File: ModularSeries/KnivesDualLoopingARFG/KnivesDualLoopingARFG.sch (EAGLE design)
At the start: 73 parts, among them P1 2XWIREPAD, P2 2XWIREPAD, P3 2XWIREPAD, P4 2XWIREPAD, Q1 2N3904, Q2 2N3904

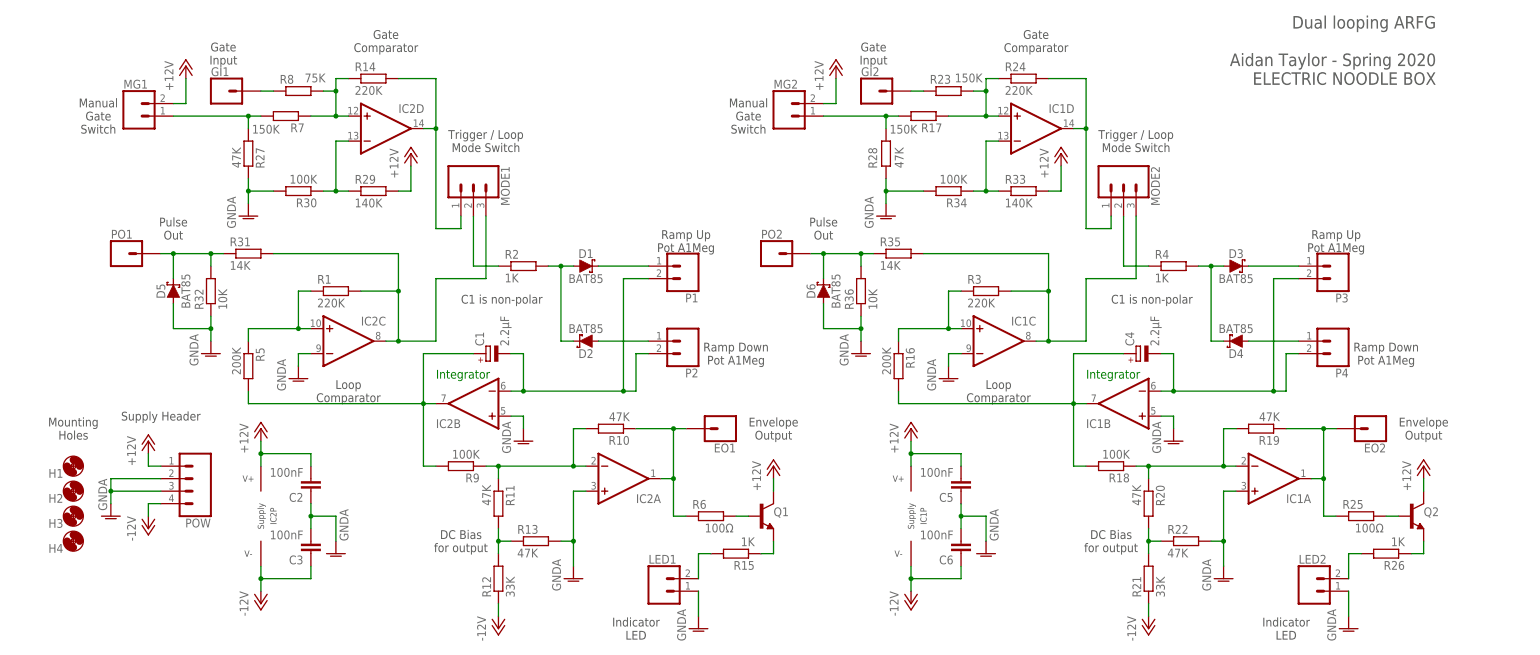
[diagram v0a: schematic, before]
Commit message: Power header updated on most PCBs. Knives layout added
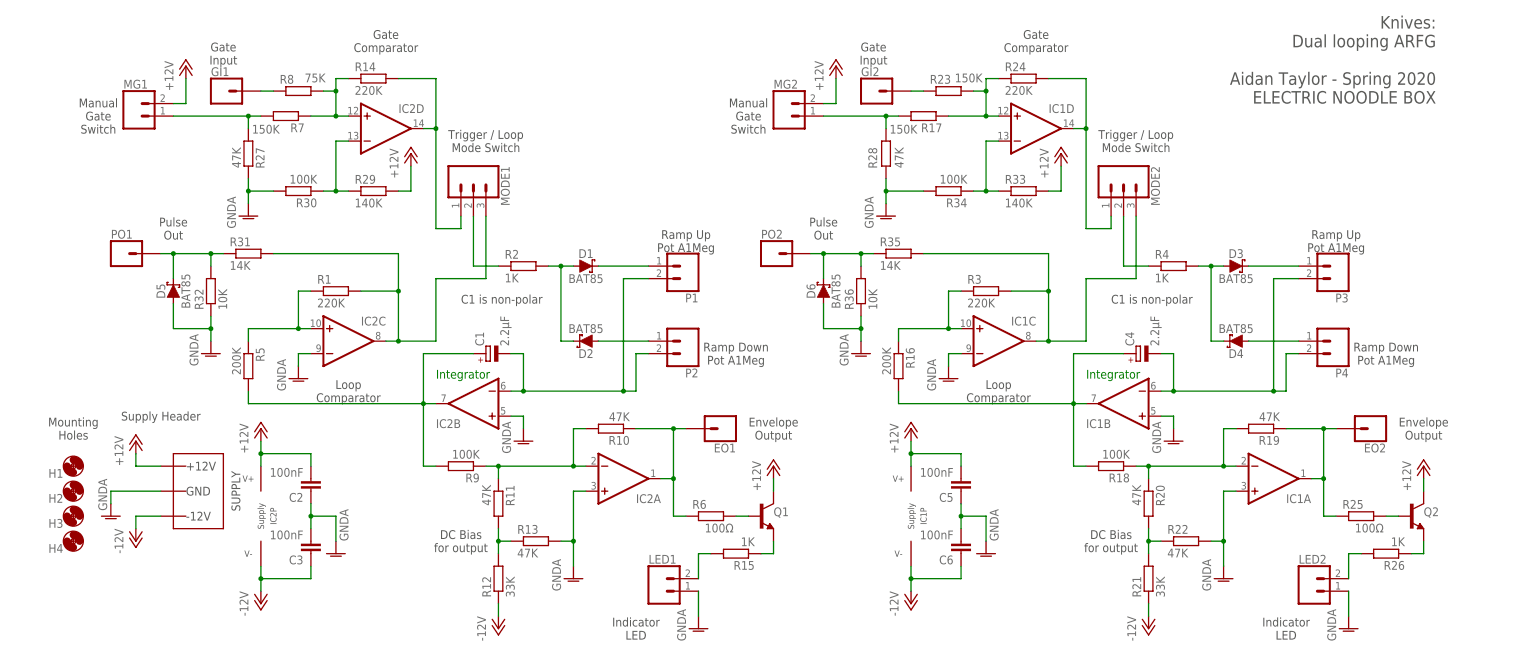
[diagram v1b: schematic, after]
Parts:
- removed POW: 4XMOLEX, ElectricNoodleBox:4XMOLEX
- added WP1: COMBO_SUPPLY_HEADER, ElectricNoodleBox:COMBO_SUPPLY_HEADER
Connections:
- net +12V: now also WP1.V++; no longer POW.1
- net -12V: now also WP1.V--; no longer POW.4
- net GNDA: now also WP1.AGND; no longer POW.2, POW.3
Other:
- note added: "Knives: Dual looping ARFG Aidan Taylor - Spring 2020 ELECTRIC NOODLE BOX"
- note removed: "Dual looping ARFG Aidan Taylor - Spring 2020 ELECTRIC NOODLE BOX"
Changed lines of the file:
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@@
 <part name="LED2" library="ElectricNoodleBox" deviceset="2XWIREPAD" device=""/>
 <part name="IC1" library="ElectricNoodleBox" deviceset="TL0X4" device="DIL" package3d_urn="urn:adsk.eagle:package:16407/2"/>
-<part name="POW" library="ElectricNoodleBox" deviceset="4XMOLEX" device="">
-<attribute name="SPICEPREFIX" value="E"/>
-</part>
 <part name="P+7" library="supply1" library_urn="urn:adsk.eagle:library:371" deviceset="+12V" device="">
 <attribute name="SPICEPREFIX" value="G"/>
@@
 <part name="GND5" library="supply1" library_urn="urn:adsk.eagle:library:371" deviceset="GNDA" device=""/>
 <part name="D6" library="ElectricNoodleBox" deviceset="SCHOTTKY_DO35" device="" package3d_urn="urn:adsk.eagle:package:43339/2" value="BAT85"/>
+<part name="WP1" library="ElectricNoodleBox" deviceset="COMBO_SUPPLY_HEADER" device=""/>
 </parts>
 <sheets>
@@
 <text x="271.78" y="50.8" size="1.778" layer="97" align="center">Envelope
 Output</text>
-<text x="274.32" y="134.62" size="2.54" layer="97" align="top-right">Dual looping ARFG
+<text x="274.32" y="134.62" size="2.54" layer="97" align="top-right">Knives:
+Dual looping ARFG
 Aidan Taylor - Spring 2020
 ELECTRIC NOODLE BOX</text>
@@
 <attribute name="NAME" x="170.18" y="33.02" size="1.27" layer="97" rot="R90" align="center"/>
 </instance>
-<instance part="POW" gate="G$1" x="20.32" y="40.64" smashed="yes" rot="R180">
-<attribute name="NAME" x="25.4" y="32.512" size="1.778" layer="95" font="vector" rot="R180"/>
-</instance>
-<instance part="P+7" gate="1" x="12.7" y="48.26" smashed="yes">
-<attribute name="VALUE" x="10.16" y="43.18" size="1.778" layer="96" rot="R90"/>
-</instance>
-<instance part="P-7" gate="1" x="12.7" y="30.48" smashed="yes">
-<attribute name="VALUE" x="10.16" y="27.94" size="1.778" layer="96" rot="R90"/>
+<instance part="P+7" gate="1" x="10.16" y="48.26" smashed="yes">
+<attribute name="VALUE" x="7.62" y="43.18" size="1.778" layer="96" rot="R90"/>
+</instance>
+<instance part="P-7" gate="1" x="10.16" y="27.94" smashed="yes">
+<attribute name="VALUE" x="7.62" y="25.4" size="1.778" layer="96" rot="R90"/>
 </instance>
 <instance part="GND13" gate="1" x="5.08" y="33.02" smashed="yes">
@@
 <attribute name="VALUE" x="152.4" y="78.74" size="1.778" layer="96" font="vector" rot="R90" align="center"/>
 </instance>
+<instance part="WP1" gate="G$1" x="22.86" y="38.1" smashed="yes"/>
 </instances>
 <busses>
@@
 </segment>
 <segment>
-<pinref part="POW" gate="G$1" pin="2"/>
-<wire x1="15.24" y1="40.64" x2="5.08" y2="40.64" width="0.1524" layer="91"/>
 <pinref part="GND13" gate="1" pin="GNDA"/>
-<wire x1="5.08" y1="40.64" x2="5.08" y2="38.1" width="0.1524" layer="91"/>
-<pinref part="POW" gate="G$1" pin="3"/>
 <wire x1="5.08" y1="38.1" x2="5.08" y2="35.56" width="0.1524" layer="91"/>
 <wire x1="15.24" y1="38.1" x2="5.08" y2="38.1" width="0.1524" layer="91"/>
-<junction x="5.08" y="38.1"/>
+<pinref part="WP1" gate="G$1" pin="AGND"/>
 </segment>
 <segment>
@@
 </segment>
 <segment>
-<pinref part="POW" gate="G$1" pin="4"/>
-<wire x1="15.24" y1="35.56" x2="12.7" y2="35.56" width="0.1524" layer="91"/>
+<wire x1="15.24" y1="33.02" x2="10.16" y2="33.02" width="0.1524" layer="91"/>
 <pinref part="P-7" gate="1" pin="-12V"/>
-<wire x1="12.7" y1="35.56" x2="12.7" y2="33.02" width="0.1524" layer="91"/>
+<wire x1="10.16" y1="33.02" x2="10.16" y2="30.48" width="0.1524" layer="91"/>
+<pinref part="WP1" gate="G$1" pin="V--"/>
 </segment>
 </net>
@@
 </segment>
 <segment>
-<pinref part="POW" gate="G$1" pin="1"/>
-<wire x1="15.24" y1="43.18" x2="12.7" y2="43.18" width="0.1524" layer="91"/>
+<wire x1="15.24" y1="43.18" x2="10.16" y2="43.18" width="0.1524" layer="91"/>
 <pinref part="P+7" gate="1" pin="+12V"/>
-<wire x1="12.7" y1="43.18" x2="12.7" y2="45.72" width="0.1524" layer="91"/>
-</segment>
-<segment>
+<wire x1="10.16" y1="43.18" x2="10.16" y2="45.72" width="0.1524" layer="91"/>
+<pinref part="WP1" gate="G$1" pin="V++"/>
+</segment>
+<segment>

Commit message: Knives documentation and BOM complete
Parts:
- added GND: 2XWIREPAD, ElectricNoodleBox:2XWIREPAD
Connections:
- net GNDA: now also GND.1, GND.2
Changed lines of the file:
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@@
 <part name="D6" library="ElectricNoodleBox" deviceset="SCHOTTKY_DO35" device="" package3d_urn="urn:adsk.eagle:package:43339/2" value="BAT85"/>
 <part name="WP1" library="ElectricNoodleBox" deviceset="COMBO_SUPPLY_HEADER" device=""/>
+<part name="GND" library="ElectricNoodleBox" deviceset="2XWIREPAD" device=""/>
+<part name="GND16" library="supply1" library_urn="urn:adsk.eagle:library:371" deviceset="GNDA" device="">
+<attribute name="SPICEPREFIX" value="G"/>
+</part>
 </parts>
 <sheets>
@@
 </instance>
 <instance part="WP1" gate="G$1" x="22.86" y="38.1" smashed="yes"/>
+<instance part="GND" gate="G$1" x="25.4" y="20.32" smashed="yes" rot="R180">
+<attribute name="NAME" x="27.94" y="14.732" size="1.778" layer="95" font="vector" rot="R180"/>
+</instance>
+<instance part="GND16" gate="1" x="15.24" y="12.7" smashed="yes">
+<attribute name="VALUE" x="12.7" y="20.32" size="1.778" layer="96" rot="R270"/>
+</instance>
 </instances>
 <busses>
@@
 <wire x1="149.86" y1="71.12" x2="149.86" y2="76.2" width="0.1524" layer="91"/>
 </segment>
+<segment>
+<pinref part="GND16" gate="1" pin="GNDA"/>
+<wire x1="15.24" y1="15.24" x2="15.24" y2="17.78" width="0.1524" layer="91"/>
+<pinref part="GND" gate="G$1" pin="1"/>
+<wire x1="15.24" y1="17.78" x2="15.24" y2="20.32" width="0.1524" layer="91"/>
+<wire x1="15.24" y1="20.32" x2="17.78" y2="20.32" width="0.1524" layer="91"/>
+<pinref part="GND" gate="G$1" pin="2"/>
+<wire x1="17.78" y1="17.78" x2="15.24" y2="17.78" width="0.1524" layer="91"/>
+<junction x="15.24" y="17.78"/>
+</segment>
 </net>

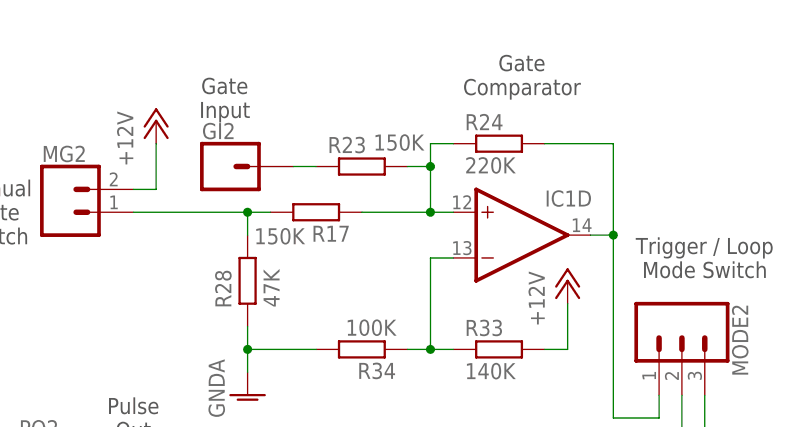
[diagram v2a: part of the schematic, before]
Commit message: Schematic and Layout fixes to Knives, TimeSeed and Portals
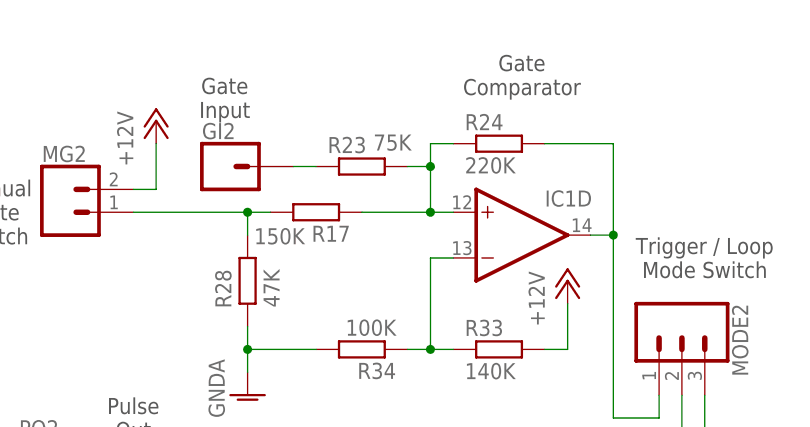
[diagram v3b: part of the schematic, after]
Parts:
- R23: value 150K -> 75K
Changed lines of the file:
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@@
 <part name="C5" library="rcl" library_urn="urn:adsk.eagle:library:334" deviceset="C-EU" device="050-025X075" package3d_urn="urn:adsk.eagle:package:23637/1" value="100nF"/>
 <part name="C6" library="rcl" library_urn="urn:adsk.eagle:library:334" deviceset="C-EU" device="050-025X075" package3d_urn="urn:adsk.eagle:package:23637/1" value="100nF"/>
-<part name="R23" library="rcl" library_urn="urn:adsk.eagle:library:334" deviceset="R-EU_" device="0207/10" package3d_urn="urn:adsk.eagle:package:23491/2" value="150K"/>
+<part name="R23" library="rcl" library_urn="urn:adsk.eagle:library:334" deviceset="R-EU_" device="0207/10" package3d_urn="urn:adsk.eagle:package:23491/2" value="75K"/>
 <part name="P+5" library="supply1" library_urn="urn:adsk.eagle:library:371" deviceset="+12V" device=""/>
 <part name="R24" library="rcl" library_urn="urn:adsk.eagle:library:334" deviceset="R-EU_" device="0207/10" package3d_urn="urn:adsk.eagle:package:23491/2" value="220K"/>
